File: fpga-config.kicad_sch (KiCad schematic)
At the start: 34 parts, among them J1 PinHeader_2x7_P2mm_SMD_Shroud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, Q1 BSS138PW, Q2 BSS138PW, Q3 BSS138PW, SW1 CVS-03B, SW2 SW_KMR211NGLFS_SMD, U2 TPD4E05U06QDQARQ1, U30 REF3012AIDBZT, U34 XCAU25P-2FFVB676I, U35 TMP451AIDQFR

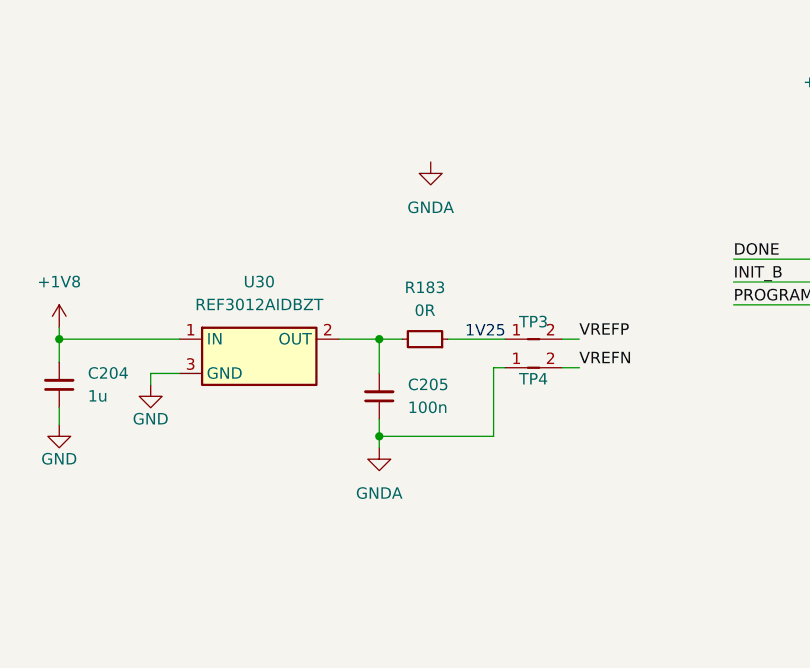
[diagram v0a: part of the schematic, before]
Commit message: [#66311] Connect 1V25 VREF negative signal to GND
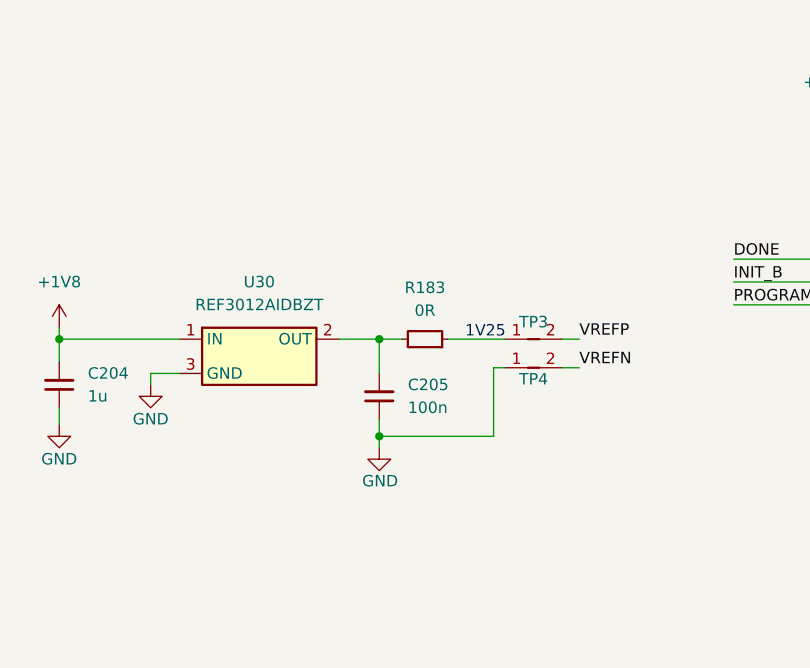
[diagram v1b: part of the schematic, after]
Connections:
- net GND: now also C205.1, TP4.1
- net GNDA: no longer C205.1, TP4.1
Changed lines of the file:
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@@
-    )
-  )
-  (symbol (lib_id "antmicropower:GNDA") (at 121.285 95.885 0) (unit 1)
-    (in_bom yes) (on_board yes) (dnp no) (fields_autoplaced)
-    (property "Reference" "#PWR018" (at 121.285 102.235 0)
-      (effects (font (size 1.27 1.27)) hide)
-    )
-    (property "Value" "GNDA" (at 121.285 100.965 0)
-      (effects (font (size 1.27 1.27)))
-    )
-    (property "Footprint" "" (at 121.285 95.885 0)
-      (effects (font (size 1.27 1.27)) hide)
-    )
-    (property "Datasheet" "" (at 121.285 95.885 0)
-      (effects (font (size 1.27 1.27)) hide)
-    )
-    (pin "1")
-    (instances
-      (project "data-center-rdimm-ddr5-tester"
-        (path "/1faa6543-e26a-4449-8bac-ee14b9f19e5f/00000000-0000-0000-0000-00005fd53c7d"
-          (reference "#PWR018") (unit 1)
-        )
-      )
     )
   )
@@
         (path "/1faa6543-e26a-4449-8bac-ee14b9f19e5f/00000000-0000-0000-0000-00005fd53c7d"
           (reference "#PWR0372") (unit 1)
+        )
+      )
+    )
+  )
+  (symbol (lib_id "antmicropower:GND") (at 121.285 95.885 0) (unit 1)
+    (in_bom yes) (on_board yes) (dnp no) (fields_autoplaced)
+    (property "Reference" "#PWR018" (at 121.285 102.235 0)
+      (effects (font (size 1.27 1.27)) hide)
+    )
+    (property "Value" "GND" (at 119.38 100.33 0)
+      (effects (font (size 1.27 1.27) (thickness 0.15)) (justify left bottom))
+    )
+    (property "Footprint" "" (at 130.175 103.505 0)
+      (effects (font (size 1.27 1.27) (thickness 0.15)) (justify left bottom) hide)
+    )
+    (property "Datasheet" "" (at 130.175 108.585 0)
+      (effects (font (size 1.27 1.27) (thickness 0.15)) (justify left bottom) hide)
+    )
+    (property "Author" "Antmicro" (at 130.175 100.965 0)
+      (effects (font (size 1.27 1.27) (thickness 0.15)) (justify left bottom) hide)
+    )
+    (property "License" "Apache-2.0" (at 130.175 103.505 0)
+      (effects (font (size 1.27 1.27) (thickness 0.15)) (justify left bottom) hide)
+    )
+    (pin "1")
+    (instances
+      (project "data-center-rdimm-ddr5-tester"
+        (path "/1faa6543-e26a-4449-8bac-ee14b9f19e5f/00000000-0000-0000-0000-00005fd53c7d"
+          (reference "#PWR018") (unit 1)
         )
       )
@@
         )
       )
-    )
-  )
-  (symbol (lib_id "antmicropower:GNDA") (at 127 64.135 0) (unit 1)
-    (in_bom yes) (on_board yes) (dnp no) (fields_autoplaced)
-    (property "Reference" "#PWR0373" (at 127 70.485 0)
-      (effects (font (size 1.27 1.27)) hide)
-    )
-    (property "Value" "GNDA" (at 127 69.215 0)
-      (effects (font (size 1.27 1.27)))
-    )
-    (property "Footprint" "" (at 127 64.135 0)
-      (effects (font (size 1.27 1.27)) hide)
-    )
-    (property "Datasheet" "" (at 127 64.135 0)
-      (effects (font (size 1.27 1.27)) hide)
-    )
-    (pin "1")
-    (instances
-      (project "data-center-rdimm-ddr5-tester"
-        (path "/1faa6543-e26a-4449-8bac-ee14b9f19e5f/00000000-0000-0000-0000-00005fd53c7d"
-          (reference "#PWR0373") (unit 1)
-        )
-      )

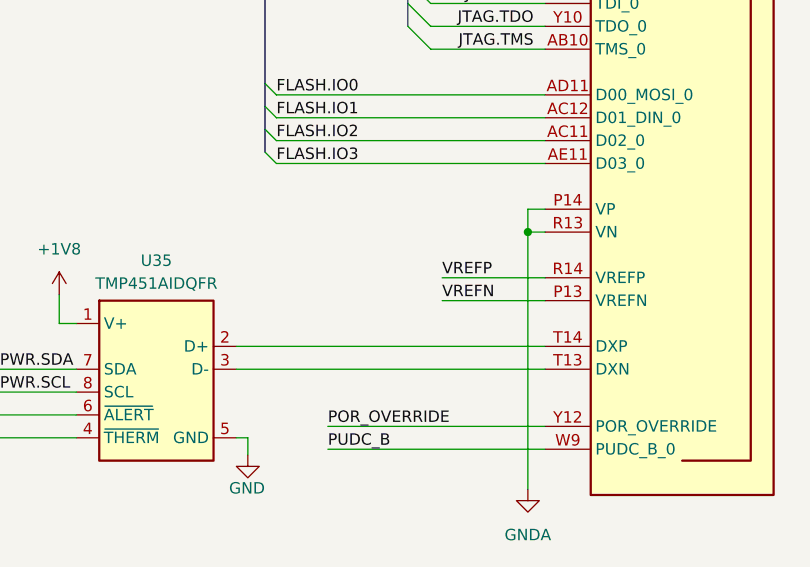
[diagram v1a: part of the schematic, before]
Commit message: [#67115] Place decoupling under FPGA
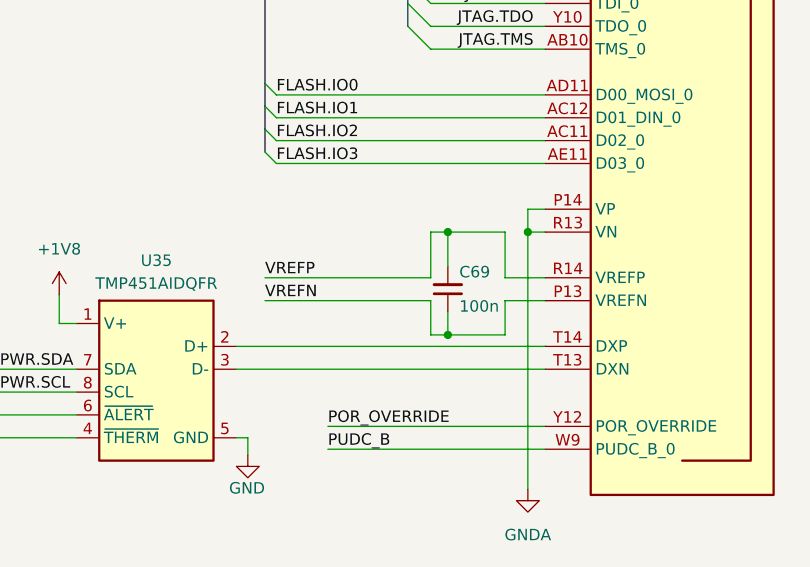
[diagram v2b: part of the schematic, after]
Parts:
- added C69: C_100n_0402, antmicro-footprints:C_0402_1005Metric_EIA, symbol antmicroCapacitors0402:C_100n_0402
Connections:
- net VREFN: now also C69.1
- net VREFP: now also C69.2
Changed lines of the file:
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@@
   (junction (at 81.28 173.355) (diameter 0) (color 0 0 0 0)
   )
+  (junction (at 313.055 137.795) (diameter 0) (color 0 0 0 0)
+  )
   (junction (at 170.815 62.23) (diameter 0) (color 0 0 0 0)
   )
@@
   (junction (at 179.07 85.09) (diameter 0) (color 0 0 0 0)
   )
+  (junction (at 313.055 149.225) (diameter 0) (color 0 0 0 0)
+  )
   (no_connect (at 42.545 242.57))
   (no_connect (at 42.545 240.03))
@@
     (stroke (width 0) (type default))
   )
+  (wire (pts (xy 313.055 137.795) (xy 313.055 141.605))
+    (stroke (width 0) (type default))
+  )
   (wire (pts (xy 164.465 226.06) (xy 164.465 227.33))
     (stroke (width 0) (type default))
@@
     (stroke (width 0) (type default))
   )
+  (wire (pts (xy 311.15 137.795) (xy 311.15 142.875))
+    (stroke (width 0) (type default))
+  )
   (wire (pts (xy 347.345 220.98) (xy 347.345 223.52))
     (stroke (width 0) (type default))
@@
     (stroke (width 0) (type default))
   )
+  (wire (pts (xy 313.055 146.685) (xy 313.055 149.225))
+    (stroke (width 0) (type default))
+  )
   (wire (pts (xy 81.28 173.355) (xy 88.9 173.355))
     (stroke (width 0) (type default))
@@
     (stroke (width 0) (type default))
   )
-  (wire (pts (xy 312.42 142.875) (xy 323.85 142.875))
+  (wire (pts (xy 323.85 102.235) (xy 313.055 102.235))
     (stroke (width 0) (type default))
   )
-  (wire (pts (xy 323.85 102.235) (xy 313.055 102.235))
+  (wire (pts (xy 319.405 145.415) (xy 323.85 145.415))
     (stroke (width 0) (type default))
   )
@@
     (stroke (width 0) (type default))
   )
+  (wire (pts (xy 319.405 142.875) (xy 319.405 137.795))
+    (stroke (width 0) (type default))
+  )
   (wire (pts (xy 179.07 97.155) (xy 181.61 97.155))
     (stroke (width 0) (type default))
@@
     (stroke (width 0) (type default))
   )
+  (wire (pts (xy 319.405 149.225) (xy 319.405 145.415))
+    (stroke (width 0) (type default))
+  )
   (wire (pts (xy 85.725 83.82) (xy 99.06 83.82))
     (stroke (width 0) (type default))
@@
     (stroke (width 0) (type default))
   )
-  (wire (pts (xy 312.42 145.415) (xy 323.85 145.415))
+  (wire (pts (xy 292.735 145.415) (xy 311.15 145.415))
     (stroke (width 0) (type default))
   )
@@
     (stroke (width 0) (type default))
   )
+  (wire (pts (xy 313.055 137.795) (xy 311.15 137.795))
+    (stroke (width 0) (type default))
+  )
   (wire (pts (xy 121.285 94.615) (xy 133.985 94.615))
     (stroke (width 0) (type default))
@@
     (stroke (width 0) (type default))
   )
+  (wire (pts (xy 311.15 149.225) (xy 313.055 149.225))
+    (stroke (width 0) (type default))
+  )
   (wire (pts (xy 181.61 86.36) (xy 181.61 85.09))
     (stroke (width 0) (type default))
@@
     (stroke (width 0) (type default))
   )
+  (wire (pts (xy 311.15 145.415) (xy 311.15 149.225))
+    (stroke (width 0) (type default))
+  )
   (wire (pts (xy 323.85 135.255) (xy 321.945 135.255))
     (stroke (width 0) (type default))
@@
     (stroke (width 0) (type default))
   )
+  (wire (pts (xy 319.405 142.875) (xy 323.85 142.875))
+    (stroke (width 0) (type default))
+  )
   (wire (pts (xy 257.81 153.035) (xy 271.78 153.035))
     (stroke (width 0) (type default))
@@
     (stroke (width 0) (type default))
   )
+  (wire (pts (xy 319.405 137.795) (xy 313.055 137.795))
+    (stroke (width 0) (type default))
+  )
   (wire (pts (xy 81.28 161.29) (xy 81.28 163.957))
     (stroke (width 0) (type default))
@@
     (stroke (width 0) (type default))
   )
+  (wire (pts (xy 313.055 149.225) (xy 319.405 149.225))
+    (stroke (width 0) (type default))
+  )
   (wire (pts (xy 155.575 251.46) (xy 156.845 251.46))
     (stroke (width 0) (type default))
@@
     (stroke (width 0) (type default))
   )
+  (wire (pts (xy 292.735 142.875) (xy 311.15 142.875))
+    (stroke (width 0) (type default))
+  )
   (wire (pts (xy 294.005 125.095) (xy 323.85 125.095))
     (stroke (width 0) (type default))
@@
     (effects (font (size 1.27 1.27)) (justify right bottom))
   )
-  (label "VREFP" (at 312.42 142.875 0) (fields_autoplaced)
+  (label "VREFP" (at 292.735 142.875 0) (fields_autoplaced)
     (effects (font (size 1.27 1.27)) (justify left bottom))
   )
@@
     (effects (font (size 1.27 1.27)) (justify left bottom))
   )
-  (label "VREFN" (at 312.42 145.415 0) (fields_autoplaced)
+  (label "VREFN" (at 292.735 145.415 0) (fields_autoplaced)
     (effects (font (size 1.27 1.27)) (justify left bottom))
   )
@@
         )
       )
+    )
+  )
+  (symbol (lib_id "antmicroCapacitors0402:C_100n_0402") (at 313.055 146.685 90) (unit 1)
+    (in_bom yes) (on_board yes) (dnp no)
+    (property "Reference" "C69" (at 314.325 142.24 90)
+      (effects (font (size 1.27 1.27)) (justify right))
+    )
+    (property "Value" "C_100n_0402" (at 323.215 126.365 0)
+      (effects (font (size 1.27 1.27) (thickness 0.15)) (justify left bottom) hide)
+    )
+    (property "Footprint" "antmicro-footprints:C_0402_1005Metric_EIA" (at 325.755 126.365 0)
+      (effects (font (size 1.27 1.27) (thickness 0.15)) (justify left bottom) hide)
+    )
+    (property "Datasheet" "https://www.murata.com/products/productdetail?partno=GRM155R61H104KE14%23" (at 328.295 126.365 0)
+      (effects (font (size 1.27 1.27) (thickness 0.15)) (justify left bottom) hide)
+    )
+    (property "Manufacturer" "Murata" (at 333.375 126.365 0)
+      (effects (font (size 1.27 1.27) (thickness 0.15)) (justify left bottom) hide)
+    )
+    (property "MPN" "GRM155R61H104KE14D" (at 330.835 126.365 0)
+      (effects (font (size 1.27 1.27) (thickness 0.15)) (justify left bottom) hide)
+    )
+    (property "Val" "100n" (at 314.325 146.05 90)
+      (effects (font (size 1.27 1.27) (thickness 0.15)) (justify right))
+    )
+    (property "License" "Apache-2.0" (at 335.915 126.365 0)
+      (effects (font (size 1.27 1.27) (thickness 0.15)) (justify left bottom) hide)
+    )
+    (property "Author" "Antmicro" (at 338.455 126.365 0)
+      (effects (font (size 1.27 1.27) (thickness 0.15)) (justify left bottom) hide)
+    )
+    (property "Voltage" "50V" (at 340.995 126.365 0)
+      (effects (font (size 1.27 1.27)) (justify left bottom) hide)
+    )
+    (property "Dielectric" "X5R" (at 343.535 126.365 0)
+      (effects (font (size 1.27 1.27)) (justify left bottom) hide)
+    )
+    (pin "1")
+    (pin "2")
+    (instances
+      (project "data-center-rdimm-ddr5-tester"
+        (path "/1faa6543-e26a-4449-8bac-ee14b9f19e5f/00000000-0000-0000-0000-00005fd53c7d"
+          (reference "C69") (unit 1)
+        )
+      )

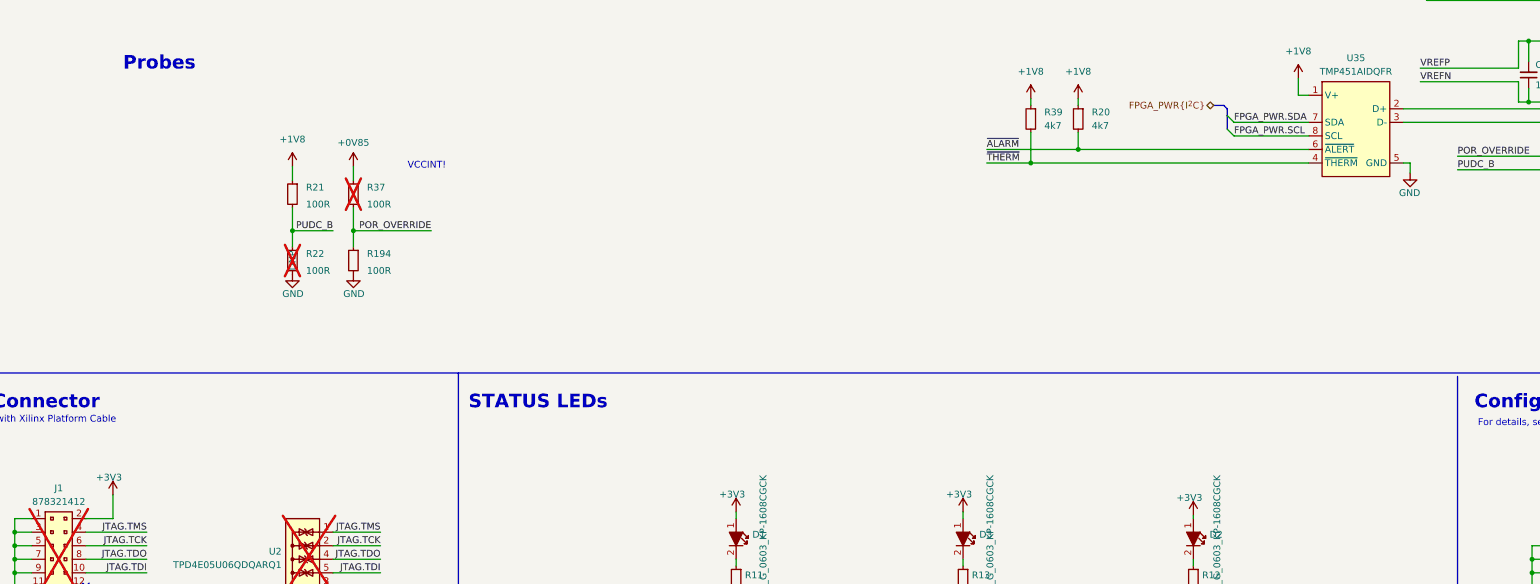
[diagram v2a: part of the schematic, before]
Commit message: [#66727] Fix schematic errors
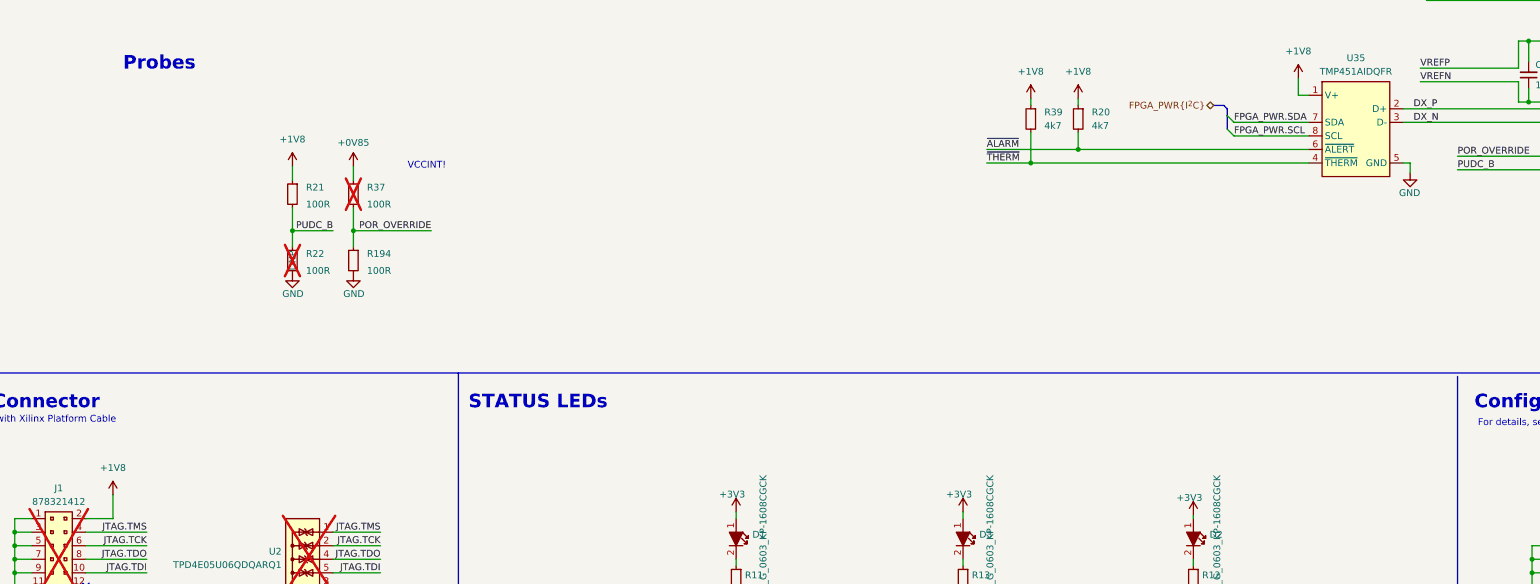
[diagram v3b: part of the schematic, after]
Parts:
- R194, R21, R22, R37: footprint antmicro-footprints:R_0402_1005Metric -> antmicro-footprints:R_0402_1005Metric_EIA
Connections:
- net +1V8: now also J1.2
- net +3V3: no longer J1.2
- net DX_P: now reaches U34.T14 (DXP), U35.2 (D+)
- net DX_N: now reaches U34.T13 (DXN), U35.3 (D-)
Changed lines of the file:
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@@
     (effects (font (size 1.27 1.27)) (justify right bottom))
+  )
+  (label "DX_N" (at 291.465 153.035 0) (fields_autoplaced)
+    (effects (font (size 1.27 1.27)) (justify left bottom))
   )
   (label "JTAG.TMS" (at 322.58 117.475 180) (fields_autoplaced)
@@
   )
   (label "PUDC_B" (at 299.72 161.925 0) (fields_autoplaced)
+    (effects (font (size 1.27 1.27)) (justify left bottom))
+  )
+  (label "DX_P" (at 291.465 150.495 0) (fields_autoplaced)
     (effects (font (size 1.27 1.27)) (justify left bottom))
   )
@@
       (effects (font (size 1.27 1.27) (thickness 0.15)) (justify left bottom) hide)
     )
-    (property "Footprint" "antmicro-footprints:R_0402_1005Metric" (at 77.47 184.277 0)
+    (property "Footprint" "antmicro-footprints:R_0402_1005Metric_EIA" (at 77.47 184.277 0)
       (effects (font (size 1.27 1.27) (thickness 0.15)) (justify left bottom) hide)
     )
@@
         (path "/1faa6543-e26a-4449-8bac-ee14b9f19e5f/00000000-0000-0000-0000-00005fd53c7d"
           (reference "R183") (unit 1)
+        )
+      )
+    )
+  )
+  (symbol (lib_id "antmicropower:+1V8") (at 47.625 222.885 0) (unit 1)
+    (in_bom yes) (on_board yes) (dnp no) (fields_autoplaced)
+    (property "Reference" "#PWR0185" (at 62.865 225.425 0)
+      (effects (font (size 1.27 1.27) (thickness 0.15)) (justify left bottom) hide)
+    )
+    (property "Value" "+1V8" (at 47.625 217.805 0)
+      (effects (font (size 1.27 1.27) (thickness 0.15)))
+    )
+    (property "Footprint" "" (at 62.865 230.505 0)
+      (effects (font (size 1.27 1.27) (thickness 0.15)) (justify left bottom) hide)
+    )
+    (property "Datasheet" "" (at 62.865 233.045 0)
+      (effects (font (size 1.27 1.27) (thickness 0.15)) (justify left bottom) hide)
+    )
+    (property "Author" "Antmicro" (at 62.865 227.965 0)
+      (effects (font (size 1.27 1.27) (thickness 0.15)) (justify left bottom) hide)
+    )
+    (property "License" "Apache-2.0" (at 62.865 230.505 0)
+      (effects (font (size 1.27 1.27) (thickness 0.15)) (justify left bottom) hide)
+    )
+    (pin "1")
+    (instances
+      (project "data-center-rdimm-ddr5-tester"
+        (path "/1faa6543-e26a-4449-8bac-ee14b9f19e5f/00000000-0000-0000-0000-00005fd53c7d"
+          (reference "#PWR0185") (unit 1)
         )
       )
@@
     )
   )
-  (symbol (lib_id "antmicropower:+3V3") (at 47.625 222.885 0) (unit 1)
-    (in_bom yes) (on_board yes) (dnp no)
-    (property "Reference" "#PWR0185" (at 47.625 226.695 0)
-      (effects (font (size 1.27 1.27)) hide)
-    )
-    (property "Value" "+3V3" (at 44.45 220.345 0)
-      (effects (font (size 1.27 1.27) (thickness 0.15)) (justify left bottom))
-    )
-    (property "Footprint" "" (at 62.865 230.505 0)
-      (effects (font (size 1.27 1.27) (thickness 0.15)) (justify left bottom) hide)
-    )
-    (property "Datasheet" "" (at 62.865 233.045 0)
-      (effects (font (size 1.27 1.27) (thickness 0.15)) (justify left bottom) hide)
-    )
-    (property "Author" "Antmicro" (at 62.865 225.425 0)
-      (effects (font (size 1.27 1.27) (thickness 0.15)) (justify left bottom) hide)
-    )
-    (property "License" "Apache-2.0" (at 62.865 227.965 0)
-      (effects (font (size 1.27 1.27) (thickness 0.15)) (justify left bottom) hide)
-    )
-    (pin "1")
-    (instances
-      (project "data-center-rdimm-ddr5-tester"
-        (path "/1faa6543-e26a-4449-8bac-ee14b9f19e5f/00000000-0000-0000-0000-00005fd53c7d"
-          (reference "#PWR0185") (unit 1)
-        )
-      )
-    )
-  )
   (symbol (lib_id "antmicroResistors0402:R_100R_0402") (at 92.71 176.403 270) (unit 1)
     (in_bom yes) (on_board yes) (dnp no)
@@
       (effects (font (size 1.27 1.27) (thickness 0.15)) (justify left bottom) hide)
     )
-    (property "Footprint" "antmicro-footprints:R_0402_1005Metric" (at 77.47 196.723 0)
+    (property "Footprint" "antmicro-footprints:R_0402_1005Metric_EIA" (at 77.47 196.723 0)
       (effects (font (size 1.27 1.27) (thickness 0.15)) (justify left bottom) hide)
     )
@@
       (effects (font (size 1.27 1.27) (thickness 0.15)) (justify left bottom) hide)
     )
-    (property "Footprint" "antmicro-footprints:R_0402_1005Metric" (at 66.04 184.277 0)
+    (property "Footprint" "antmicro-footprints:R_0402_1005Metric_EIA" (at 66.04 184.277 0)
       (effects (font (size 1.27 1.27) (thickness 0.15)) (justify left bottom) hide)
     )
@@
       (effects (font (size 1.27 1.27) (thickness 0.15)) (justify left bottom) hide)
     )
-    (property "Footprint" "antmicro-footprints:R_0402_1005Metric" (at 66.04 196.723 0)
-      (effects (font (size 1.27 1.27) (thickness 0.15)) (justify left bottom) hide)
-    )
+    (property "Footprint" "antmicro-footprints:R_0402_1005Metric_EIA" (at 66.04 196.723 0)
+      (effects (font (size 1.27 1.27) (thickness 0.15)) (justify left bottom) hide)
+    )
